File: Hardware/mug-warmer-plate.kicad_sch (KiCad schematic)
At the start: 36 parts, among them J1 USB_C_Receptacle_USB2.0, J4 Conn_01x02_Male, Q1 IRLZ44N, SW1 SW_DIP_x01, U1 LM35-NEB, U2 ATtiny85-20P

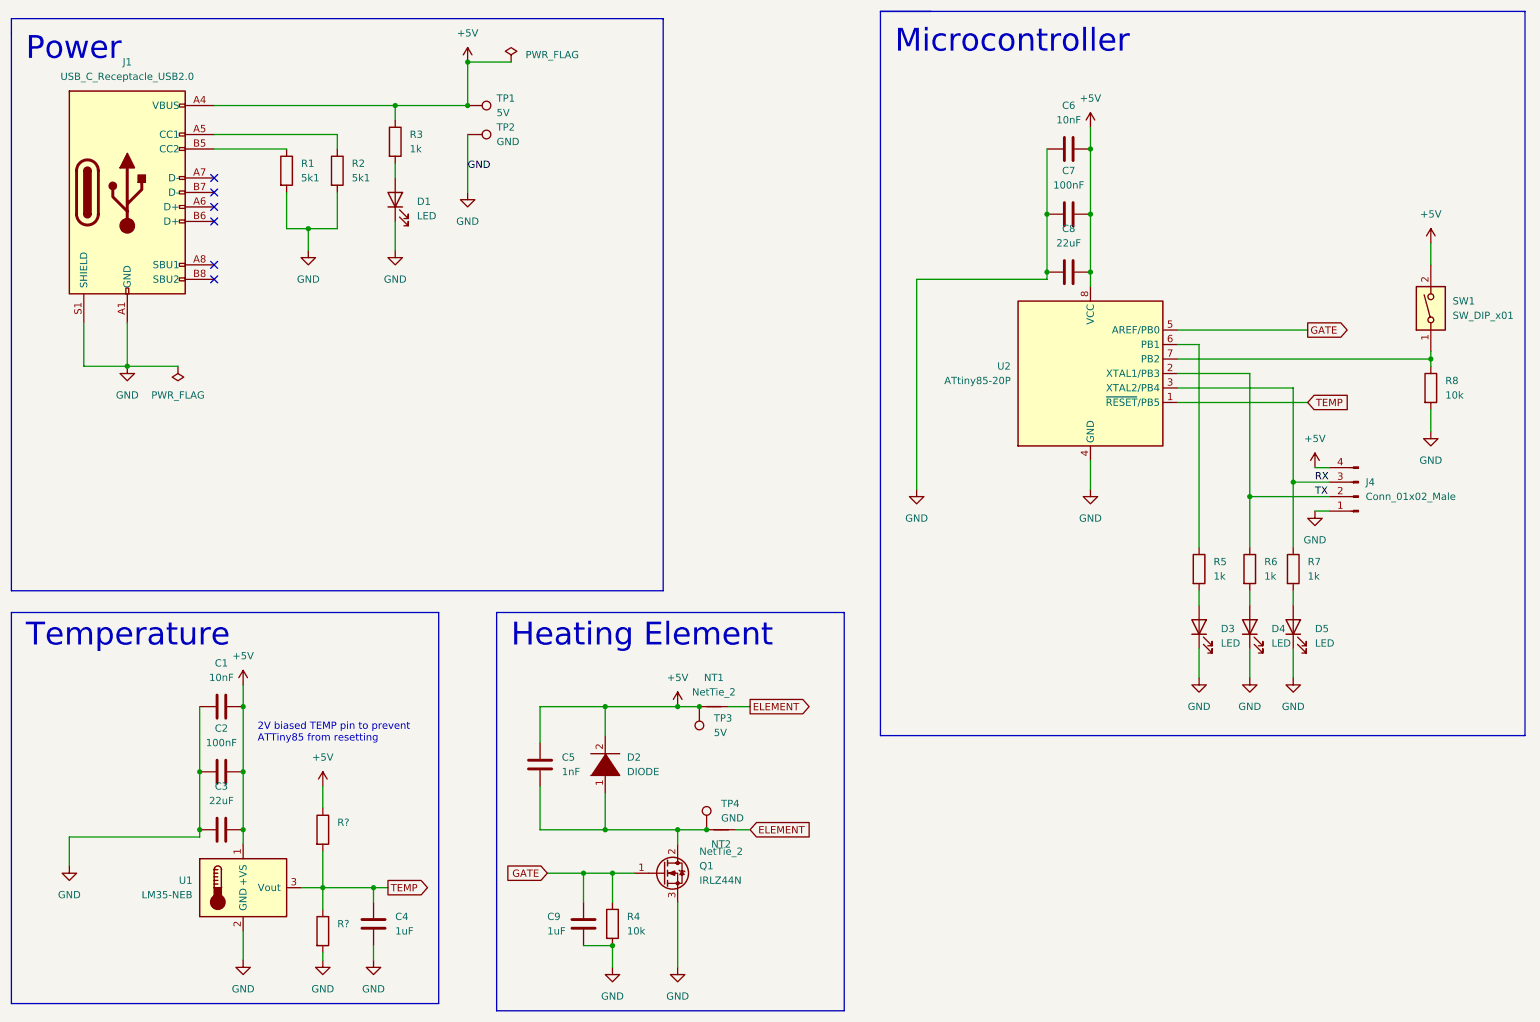
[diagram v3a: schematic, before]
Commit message: Use ATTiny85 internal pullup resistor for switch
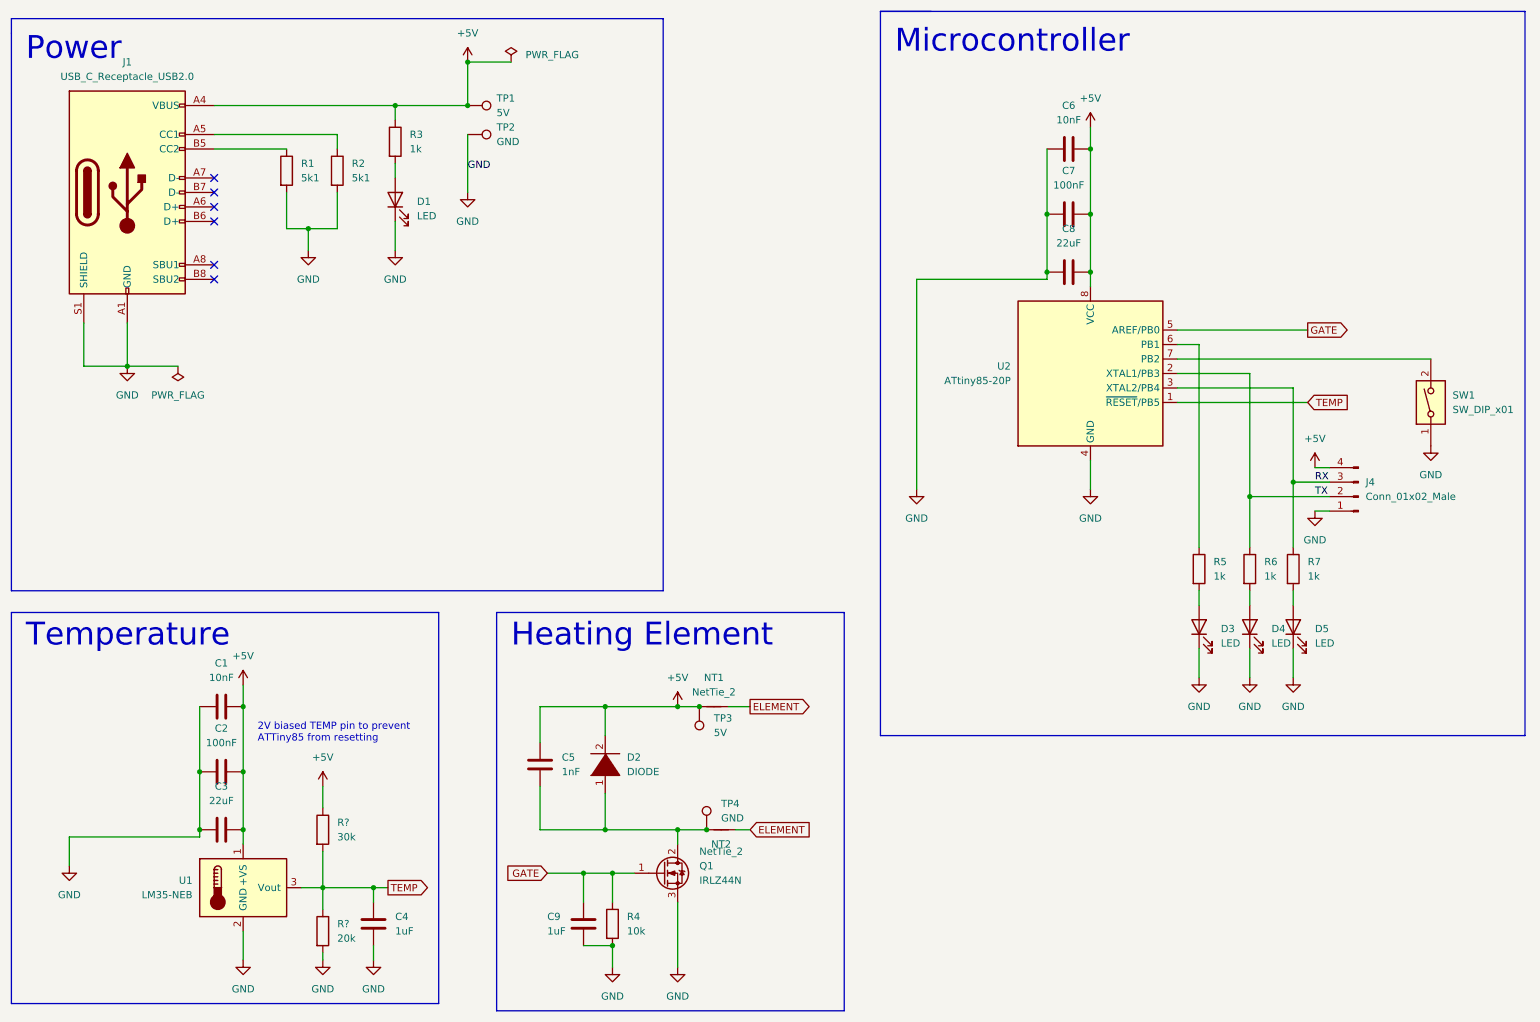
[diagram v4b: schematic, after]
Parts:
- removed R8: 10k, Resistor_THT:R_Axial_DIN0207_L6.3mm_D2.5mm_P10.16mm_Horizontal, symbol Device:R
- R?: value (none) -> 30k
- R?: value (none) -> 20k
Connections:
- net +5V: no longer SW1.2
- net GND: now also SW1.1
- net at U2.7 (PB2): now also SW1.2; no longer SW1.1
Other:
- moved on the sheet: SW1
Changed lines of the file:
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@@
   (junction (at 234.95 104.14) (diameter 0) (color 0 0 0 0)
-  )
-  (junction (at 266.7 80.01) (diameter 0) (color 0 0 0 0)
   )
   (junction (at 50.8 162.56) (diameter 0) (color 0 0 0 0)
@@
     (stroke (width 0) (type default) (color 0 0 0 0))
   )
-  (wire (pts (xy 266.7 88.9) (xy 266.7 92.71))
-    (stroke (width 0) (type default) (color 0 0 0 0))
-  )
   (wire (pts (xy 207.01 54.61) (xy 207.01 64.77))
     (stroke (width 0) (type default) (color 0 0 0 0))
@@
     (stroke (width 0) (type default) (color 0 0 0 0))
   )
-  (wire (pts (xy 266.7 80.01) (xy 266.7 78.74))
-    (stroke (width 0) (type default) (color 0 0 0 0))
-  )
   (wire (pts (xy 38.1 73.66) (xy 38.1 81.28))
     (stroke (width 0) (type default) (color 0 0 0 0))
@@
     (stroke (width 0) (type default) (color 0 0 0 0))
   )
-  (wire (pts (xy 266.7 80.01) (xy 266.7 81.28))
-    (stroke (width 0) (type default) (color 0 0 0 0))
-  )
   (polyline (pts (xy 102.87 124.46) (xy 163.83 124.46))
     (stroke (width 0) (type default) (color 0 0 0 0))
@@
   )
   (wire (pts (xy 58.42 162.56) (xy 58.42 165.1))
-    (stroke (width 0) (type default) (color 0 0 0 0))
-  )
-  (wire (pts (xy 266.7 59.69) (xy 266.7 63.5))
     (stroke (width 0) (type default) (color 0 0 0 0))
   )
@@
     (pin "2")
   )
-  (symbol (lib_id "power:+5V") (at 266.7 59.69 0) (unit 1)
-    (in_bom yes) (on_board yes)
-    (property "Reference" "#PWR019" (id 0) (at 266.7 63.5 0)
-      (effects (font (size 1.27 1.27)) hide)
-    )
-    (property "Value" "+5V" (id 1) (at 266.7 54.61 0))
-    (property "Footprint" "" (id 2) (at 266.7 59.69 0)
-      (effects (font (size 1.27 1.27)) hide)
-    )
-    (property "Datasheet" "" (id 3) (at 266.7 59.69 0)
-      (effects (font (size 1.27 1.27)) hide)
-    )
-    (pin "1")
-  )
   (symbol (lib_id "power:PWR_FLAG") (at 105.41 27.94 0) (unit 1)
     (in_bom yes) (on_board yes) (fields_autoplaced)
@@
     (pin "4")
   )
-  (symbol (lib_id "power:GND") (at 266.7 92.71 0) (unit 1)
-    (in_bom yes) (on_board yes) (fields_autoplaced)
-    (property "Reference" "#PWR020" (id 0) (at 266.7 99.06 0)
-      (effects (font (size 1.27 1.27)) hide)
-    )
-    (property "Value" "GND" (id 1) (at 266.7 97.79 0))
-    (property "Footprint" "" (id 2) (at 266.7 92.71 0)
-      (effects (font (size 1.27 1.27)) hide)
-    )
-    (property "Datasheet" "" (id 3) (at 266.7 92.71 0)
+  (symbol (lib_id "power:GND") (at 266.7 95.25 0) (unit 1)
+    (in_bom yes) (on_board yes) (fields_autoplaced)
+    (property "Reference" "#PWR020" (id 0) (at 266.7 101.6 0)
+      (effects (font (size 1.27 1.27)) hide)
+    )
+    (property "Value" "GND" (id 1) (at 266.7 100.33 0))
+    (property "Footprint" "" (id 2) (at 266.7 95.25 0)
+      (effects (font (size 1.27 1.27)) hide)
+    )
+    (property "Datasheet" "" (id 3) (at 266.7 95.25 0)
       (effects (font (size 1.27 1.27)) hide)
     )
@@
     (pin "2")
   )
-  (symbol (lib_id "Switch:SW_DIP_x01") (at 266.7 71.12 90) (unit 1)
-    (in_bom yes) (on_board yes) (fields_autoplaced)
-    (property "Reference" "SW1" (id 0) (at 270.51 69.8499 90)
-      (effects (font (size 1.27 1.27)) (justify right))
-    )
-    (property "Value" "SW_DIP_x01" (id 1) (at 270.51 72.3899 90)
-      (effects (font (size 1.27 1.27)) (justify right))
-    )
-    (property "Footprint" "Button_Switch_THT:SW_PUSH_6mm_H4.3mm" (id 2) (at 266.7 71.12 0)
-      (effects (font (size 1.27 1.27)) hide)
-    )
-    (property "Datasheet" "~" (id 3) (at 266.7 71.12 0)
+  (symbol (lib_id "Switch:SW_DIP_x01") (at 266.7 87.63 90) (unit 1)
+    (in_bom yes) (on_board yes) (fields_autoplaced)
+    (property "Reference" "SW1" (id 0) (at 270.51 86.3599 90)
+      (effects (font (size 1.27 1.27)) (justify right))
+    )
+    (property "Value" "SW_DIP_x01" (id 1) (at 270.51 88.8999 90)
+      (effects (font (size 1.27 1.27)) (justify right))
+    )
+    (property "Footprint" "Button_Switch_THT:SW_PUSH_6mm_H4.3mm" (id 2) (at 266.7 87.63 0)
+      (effects (font (size 1.27 1.27)) hide)
+    )
+    (property "Datasheet" "~" (id 3) (at 266.7 87.63 0)
       (effects (font (size 1.27 1.27)) hide)
     )
@@
       (effects (font (size 1.27 1.27)) (justify left))
     )
-    (property "Value" "" (id 1) (at 74.93 163.8299 0)
+    (property "Value" "30k" (id 1) (at 74.93 163.8299 0)
       (effects (font (size 1.27 1.27)) (justify left))
     )
@@
     (pin "1")
   )
-  (symbol (lib_id "Device:R") (at 266.7 85.09 0) (unit 1)
-    (in_bom yes) (on_board yes) (fields_autoplaced)
-    (property "Reference" "R8" (id 0) (at 269.24 83.8199 0)
-      (effects (font (size 1.27 1.27)) (justify left))
-    )
-    (property "Value" "10k" (id 1) (at 269.24 86.3599 0)
-      (effects (font (size 1.27 1.27)) (justify left))
-    )
-    (property "Footprint" "Resistor_THT:R_Axial_DIN0207_L6.3mm_D2.5mm_P10.16mm_Horizontal" (id 2) (at 264.922 85.09 90)
-      (effects (font (size 1.27 1.27)) hide)
-    )
-    (property "Datasheet" "~" (id 3) (at 266.7 85.09 0)
-      (effects (font (size 1.27 1.27)) hide)
-    )
-    (pin "1")
-    (pin "2")
-  )
   (symbol (lib_id "Connector:TestPoint") (at 97.79 35.56 270) (unit 1)
     (in_bom yes) (on_board yes) (fields_autoplaced)
@@
       (effects (font (size 1.27 1.27)) (justify left))
     )
-    (property "Value" "" (id 1) (at 74.93 181.6099 0)
+    (property "Value" "20k" (id 1) (at 74.93 181.6099 0)
       (effects (font (size 1.27 1.27)) (justify left))
     )
@@
       (reference "#PWR018") (unit 1) (value "GND") (footprint "")
     )
-    (path "/13679221-fe28-4707-a3f4-c0ced2087e49"
-      (reference "#PWR019") (unit 1) (value "+5V") (footprint "")
-    )
     (path "/5f4bf74b-9d39-4442-be83-72e147880e63"
       (reference "#PWR020") (unit 1) (value "GND") (footprint "")
@@
       (reference "R7") (unit 1) (value "1k") (footprint "Resistor_THT:R_Axial_DIN0207_L6.3mm_D2.5mm_P10.16mm_Horizontal")
     )
-    (path "/e9efe5a7-24f6-46cd-b9a0-d87817d41bcc"
-      (reference "R8") (unit 1) (value "10k") (footprint "Resistor_THT:R_Axial_DIN0207_L6.3mm_D2.5mm_P10.16mm_Horizontal")
-    )
     (path "/cbf1ea5c-da65-4d09-b093-267466cb207b"
